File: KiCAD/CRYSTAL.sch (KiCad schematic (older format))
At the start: 3 parts, among them J23 Conn_01x02, J24 Conn_01x02, U8 FXO-SM7_OSC-SMD7050_short

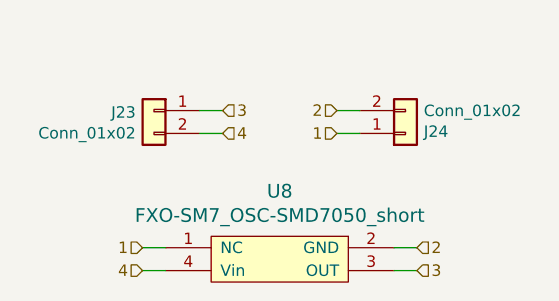
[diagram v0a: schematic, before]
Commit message: added usb, crystals
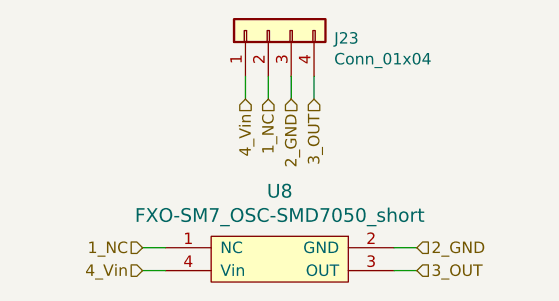
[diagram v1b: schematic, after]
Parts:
- removed J23, J24: Conn_01x02, Connector_PinHeader_2.54mm:PinHeader_1x02_P2.54mm_Vertical, symbol Connector_Generic:Conn_01x02
- added J23: Conn_01x04, Connector_PinHeader_2.54mm:PinHeader_1x04_P2.54mm_Vertical, symbol Connector_Generic:Conn_01x04
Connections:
- net 1 renamed 1_NC
- net 1_NC: now also J23.2 (Pin_2)
- net 2 renamed 2_GND
- net 2_GND: now also J23.3 (Pin_3)
- net 3 renamed 3_OUT
- net 3_OUT: now also J23.4 (Pin_4)
- net 4 renamed 4_Vin
- net 4_Vin: now also J23.1 (Pin_1)
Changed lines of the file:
@@
 $Descr A4 11693 8268
 encoding utf-8
-Sheet 9 17
+Sheet 9 18
 Title ""
 Date ""
@@
 Comment4 ""
 $EndDescr
-$Comp
-L Connector_Generic:Conn_01x02 J23
-U 1 1 5CDAD77D
-P 4850 2450
-F 0 "J23" H 4930 2442 50  0000 L CNN
-F 1 "Conn_01x02" H 4930 2351 50  0000 L CNN
-F 2 "Connector_PinHeader_2.54mm:PinHeader_1x02_P2.54mm_Vertical" H 4850 2450 50  0001 C CNN
-F 3 "~" H 4850 2450 50  0001 C CNN
-F 4 "PLS-2, PBS-2" H 4850 2450 50  0001 C CNN "MNP"
-F 5 "Kls, CONNFLY" H 4850 2450 50  0001 C CNN "Manufacturer"
-	1    4850 2450
-	-1   0    0    -1
-$EndComp
-$Comp
-L Connector_Generic:Conn_01x02 J24
-U 1 1 5CDAD7B8
-P 5950 2550
-F 0 "J24" H 6030 2542 50  0000 L CNN
-F 1 "Conn_01x02" H 6030 2451 50  0000 L CNN
-F 2 "Connector_PinHeader_2.54mm:PinHeader_1x02_P2.54mm_Vertical" H 5950 2550 50  0001 C CNN
-F 3 "~" H 5950 2550 50  0001 C CNN
-	1    5950 2550
-	1    0    0    1
-$EndComp
 $Comp
 L fxo-sm7_osc-smd7050:FXO-SM7_OSC-SMD7050_short U8
@@
 $EndComp
 Text HLabel 4800 3150 0    50   Input ~ 0
-4
+4_Vin
 Wire Wire Line
 	4800 3150 4900 3150
 Text HLabel 4800 3050 0    50   Input ~ 0
-1
+1_NC
 Wire Wire Line
 	4800 3050 4900 3050
 Text HLabel 6000 3150 2    50   Input ~ 0
-3
+3_OUT
 Wire Wire Line
 	6000 3150 5900 3150
 Text HLabel 6000 3050 2    50   Input ~ 0
-2
+2_GND
 Wire Wire Line
 	6000 3050 5900 3050
-Text HLabel 5650 2450 0    50   Input ~ 0
-2
-Text HLabel 5650 2550 0    50   Input ~ 0
-1
+Text HLabel 5450 2400 3    50   Input ~ 0
+2_GND
+Text HLabel 5350 2400 3    50   Input ~ 0
+1_NC
 Wire Wire Line
-	5650 2450 5750 2450
+	5450 2400 5450 2300
 Wire Wire Line
-	5650 2550 5750 2550
-Text HLabel 5150 2450 2    50   Input ~ 0
-3
+	5350 2400 5350 2300
+Text HLabel 5550 2400 3    50   Input ~ 0
+3_OUT
 Wire Wire Line
-	5150 2450 5050 2450
-Text HLabel 5150 2550 2    50   Input ~ 0
-4
+	5550 2400 5550 2300
+Text HLabel 5250 2400 3    50   Input ~ 0
+4_Vin
 Wire Wire Line
-	5150 2550 5050 2550
+	5250 2400 5250 2300
+$Comp
+L Connector_Generic:Conn_01x04 J23
+U 1 1 5CF546A2
+P 5350 2100
+F 0 "J23" V 5316 1812 50  0000 R CNN
+F 1 "Conn_01x04" V 5225 1812 50  0000 R CNN
+F 2 "Connector_PinHeader_2.54mm:PinHeader_1x04_P2.54mm_Vertical" H 5350 2100 50  0001 C CNN
+F 3 "~" H 5350 2100 50  0001 C CNN
+	1    5350 2100
+	0    -1   -1   0
+$EndComp
 $EndSCHEMATC
